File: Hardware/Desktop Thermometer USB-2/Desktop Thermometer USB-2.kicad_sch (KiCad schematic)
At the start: 0 parts

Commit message: Updated some symbols and footprints. Also added a new model for an epoxy type ceramic capacitor
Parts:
- added C1: C, Footprints:C_Epoxy_D5.5mm_W3.2mm_P5.00mm, symbol Schematic Symbols:C
- added J1: USB_TYPE_B, 00TH-Connector:USB_TYPE_B, symbol Schematic Symbols:USB_TYPE_B
- added R1: R, Resistor_THT:R_Axial_DIN0414_L11.9mm_D4.5mm_P15.24mm_Horizontal, symbol Device:R
- added U1: PIC16F15214, Footprints:DIP-8_W7.62mm_LongPads, symbol Schematic Symbols:PIC16F15214
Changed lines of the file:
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@@
 (kicad_sch (version 20230121) (generator eeschema)
   (paper "A4")
+  (symbol (lib_id "Schematic Symbols:USB_TYPE_B") (at 62.865 109.22 0) (unit 1)
+    (in_bom yes) (on_board yes) (dnp no) (fields_autoplaced)
+    (property "Reference" "J1" (at 62.865 96.52 0)
+      (effects (font (size 1.27 1.27)))
+    )
+    (property "Value" "USB_TYPE_B" (at 62.865 99.06 0)
+      (effects (font (size 1.27 1.27)))
+    )
+    (property "Footprint" "00TH-Connector:USB_TYPE_B" (at 62.865 133.35 0)
+      (effects (font (size 1.27 1.27)) hide)
+    )
+    (property "Datasheet" "https://www.cuidevices.com/product/resource/uj2-bh-th.pdf" (at 62.865 130.81 0)
+      (effects (font (size 1.27 1.27)) hide)
+    )
+    (pin "1")
+    (pin "2")
+    (pin "3")
+    (pin "5")
+    (pin "4")
+    (instances
+      (project "Desktop Thermometer USB-2"
+        (path "/155b486c-e28e-4d6b-9039-05edc3f4c6ee"
+          (reference "J1") (unit 1)
+        )
+      )
+    )
+  )
+  (symbol (lib_id "Schematic Symbols:PIC16F15214") (at 85.09 57.15 0) (unit 1)
+    (in_bom yes) (on_board yes) (dnp no)
+    (property "Reference" "U1" (at 78.74 46.99 0)
+      (effects (font (size 1.27 1.27)) (justify right))
+    )
+    (property "Value" "PIC16F15214" (at 91.44 67.31 0)
+      (effects (font (size 1.27 1.27)) (justify right))
+    )
+    (property "Footprint" "Footprints:DIP-8_W7.62mm_LongPads" (at 85.09 82.55 0)
+      (effects (font (size 1.27 1.27) italic) hide)
+    )
+    (property "Datasheet" "https://ww1.microchip.com/downloads/en/DeviceDoc/PIC16F15213-14-23-24-43-44-Data-Sheet-DS40002195B.pdf" (at 87.63 85.09 0)
+      (effects (font (size 1.27 1.27)) hide)
+    )
+    (pin "1")
+    (pin "6")
+    (pin "8")
+    (pin "7")
+    (pin "3")
+    (pin "2")
+    (pin "5")
+    (pin "4")
+    (instances
+      (project "Desktop Thermometer USB-2"
+        (path "/155b486c-e28e-4d6b-9039-05edc3f4c6ee"
+          (reference "U1") (unit 1)
+        )
+      )
+    )
+  )
+  (symbol (lib_id "power:GND") (at 196.85 93.98 0) (unit 1)
+    (in_bom yes) (on_board yes) (dnp no) (fields_autoplaced)
+    (property "Reference" "#PWR02" (at 196.85 100.33 0)
+      (effects (font (size 1.27 1.27)) hide)
+    )
+    (property "Value" "GND" (at 196.85 99.06 0)
+      (effects (font (size 1.27 1.27)))
+    )
+    (property "Footprint" "" (at 196.85 93.98 0)
+      (effects (font (size 1.27 1.27)) hide)
+    )
+    (property "Datasheet" "" (at 196.85 93.98 0)
+      (effects (font (size 1.27 1.27)) hide)
+    )
+    (pin "1")
+    (instances
+      (project "Desktop Thermometer USB-2"
+        (path "/155b486c-e28e-4d6b-9039-05edc3f4c6ee"
+          (reference "#PWR02") (unit 1)
+        )
+      )
+    )
+  )
+  (symbol (lib_id "Schematic Symbols:C") (at 121.92 92.71 0) (unit 1)
+    (in_bom yes) (on_board yes) (dnp no) (fields_autoplaced)
+    (property "Reference" "C1" (at 125.73 91.44 0)
+      (effects (font (size 1.27 1.27)) (justify left))
+    )
+    (property "Value" "C" (at 125.73 93.98 0)
+      (effects (font (size 1.27 1.27)) (justify left))
+    )
+    (property "Footprint" "Footprints:C_Epoxy_D5.5mm_W3.2mm_P5.00mm" (at 120.65 104.14 0)
+      (effects (font (size 1.27 1.27)) hide)
+    )
+    (property "Datasheet" "https://www.vishay.com/docs/45171/kseries.pdf" (at 120.65 106.68 0)
+      (effects (font (size 1.27 1.27)) hide)
+    )
+    (pin "1")
+    (pin "2")
+    (instances
+      (project "Desktop Thermometer USB-2"
+        (path "/155b486c-e28e-4d6b-9039-05edc3f4c6ee"
+          (reference "C1") (unit 1)
+        )
+      )
+    )
+  )
+  (symbol (lib_id "power:+5V") (at 207.645 71.12 0) (unit 1)
+    (in_bom yes) (on_board yes) (dnp no) (fields_autoplaced)
+    (property "Reference" "#PWR01" (at 207.645 74.93 0)
+      (effects (font (size 1.27 1.27)) hide)
+    )
+    (property "Value" "+5V" (at 207.645 66.04 0)
+      (effects (font (size 1.27 1.27)))
+    )
+    (property "Footprint" "" (at 207.645 71.12 0)
+      (effects (font (size 1.27 1.27)) hide)
+    )
+    (property "Datasheet" "" (at 207.645 71.12 0)
+      (effects (font (size 1.27 1.27)) hide)
+    )
+    (pin "1")
+    (instances
+      (project "Desktop Thermometer USB-2"
+        (path "/155b486c-e28e-4d6b-9039-05edc3f4c6ee"
+          (reference "#PWR01") (unit 1)
+        )
+      )
+    )
+  )
+  (symbol (lib_id "Device:R") (at 140.97 67.945 0) (unit 1)
+    (in_bom yes) (on_board yes) (dnp no) (fields_autoplaced)
+    (property "Reference" "R1" (at 143.51 66.675 0)
+      (effects (font (size 1.27 1.27)) (justify left))
+    )
+    (property "Value" "R" (at 143.51 69.215 0)
+      (effects (font (size 1.27 1.27)) (justify left))
+    )
+    (property "Footprint" "Resistor_THT:R_Axial_DIN0414_L11.9mm_D4.5mm_P15.24mm_Horizontal" (at 139.192 67.945 90)
+      (effects (font (size 1.27 1.27)) hide)
+    )
+    (property "Datasheet" "https://www.seielect.com/catalog/sei-cf_cfm.pdf" (at 140.97 67.945 0)
+      (effects (font (size 1.27 1.27)) hide)
+    )
+    (pin "1")
+    (pin "2")
+    (instances
+      (project "Desktop Thermometer USB-2"
+        (path "/155b486c-e28e-4d6b-9039-05edc3f4c6ee"
+          (reference "R1") (unit 1)
+        )
+      )
+    )
+  )
   (sheet_instances
     (path "/" (page "1"))

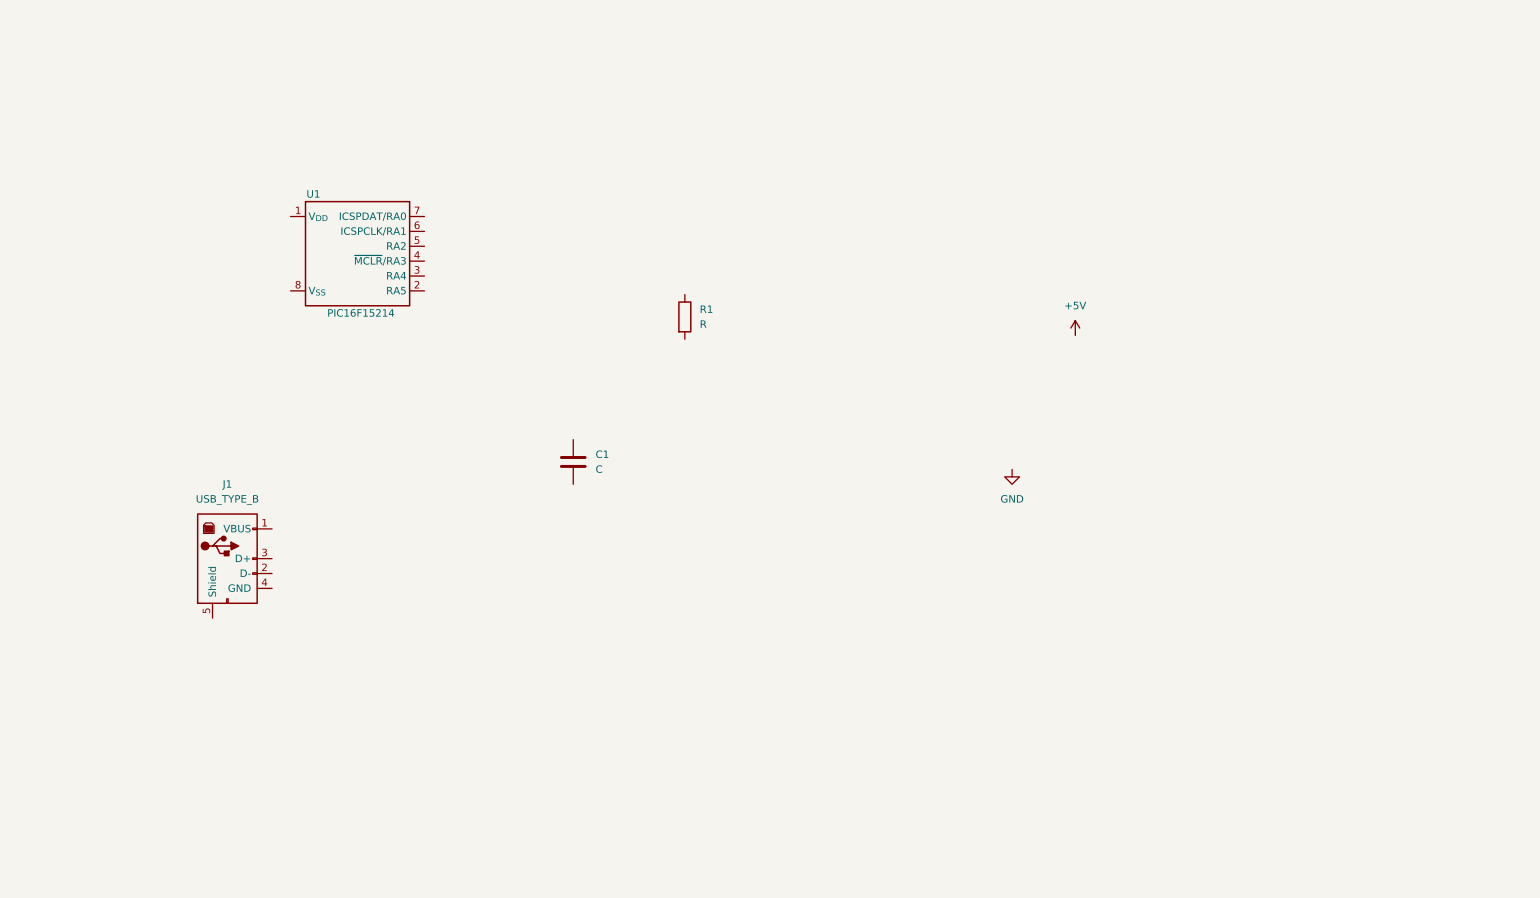
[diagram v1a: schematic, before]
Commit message: Schematic roughed out, requires a tidy up into sections. Added some more symbols and footprints...Hopefully done with that stuff!
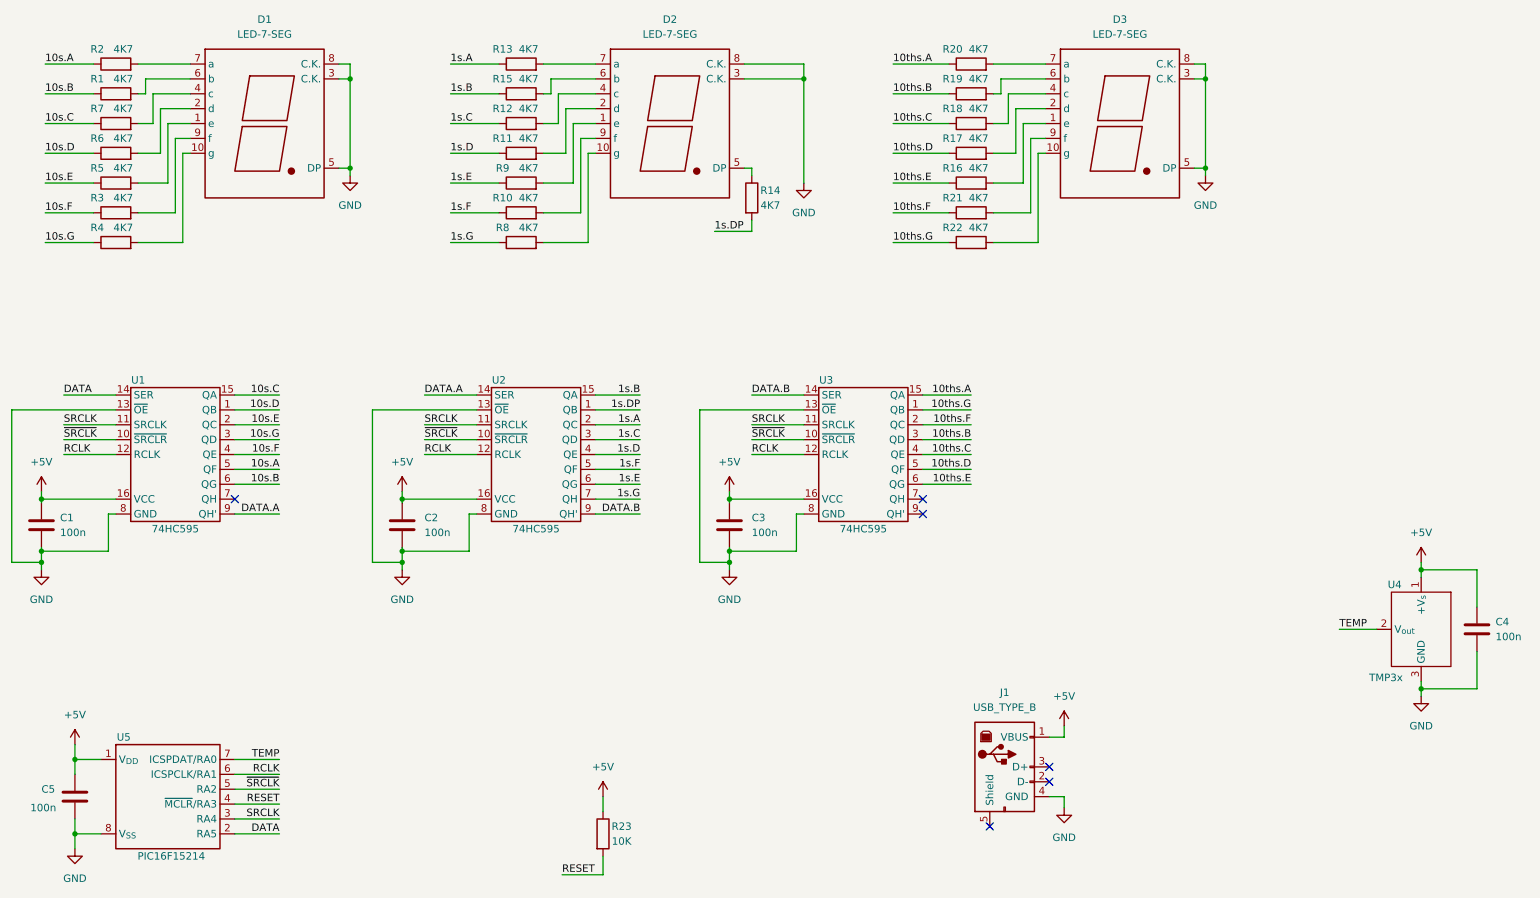
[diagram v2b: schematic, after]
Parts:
- removed U1: PIC16F15214, Footprints:DIP-8_W7.62mm_LongPads, symbol Schematic Symbols:PIC16F15214
- added C2, C3, C4, C5: 100n, Footprints:C_Epoxy_D5.5mm_W3.2mm_P5.00mm, symbol Schematic Symbols:C
- added D1, D2, D3: LED-7-SEG, Footprints:LED-7-SEG, symbol Schematic Symbols:LED-7-SEG
- added R10, R11, R12, R13, R14, R15, R16, R17, R18, R19, R2, R20, R21, R22, R3, R4, R5, R6, R7, R8, R9: 4K7, Resistor_THT:R_Axial_DIN0414_L11.9mm_D4.5mm_P15.24mm_Horizontal, symbol Device:R
- added R23: 10K, Resistor_THT:R_Axial_DIN0414_L11.9mm_D4.5mm_P15.24mm_Horizontal, symbol Device:R
- added U1, U2, U3: 74HC595, Footprints:DIP-16_W7.62mm_LongPads, symbol Schematic Symbols:74HC595
- added U4: TMP3x, Footprints:TMP3x_TO-92, symbol Schematic Symbols:TMP3x
- added U5: PIC16F15214, Footprints:DIP-8_W7.62mm_LongPads, symbol Schematic Symbols:PIC16F15214
- C1: value C -> 100n
- J1: footprint 00TH-Connector:USB_TYPE_B -> Footprints:USB_TYPE_B
- R1: value R -> 4K7
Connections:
- net +5V: now also C1.1, J1.1 (VBUS), C2.1, C3.1, C4.1, C5.1, R23.1, U1.16 (VCC), U2.16 (VCC), U3.16 (VCC), U4.1 (+V_{s}), U5.1 (V_{DD})
- net GND: now also C1.2, J1.4 (GND), C2.2, C3.2, C4.2, C5.2, D1.3 (C.K.), D1.5 (DP), D1.8 (C.K.), D2.3 (C.K.), D2.8 (C.K.), D3.3 (C.K.), D3.5 (DP), D3.8 (C.K.), U1.13 (~{OE}), U1.8 (GND), U2.13 (~{OE}), U2.8 (GND), U3.13 (~{OE}), U3.8 (GND), U4.3 (GND), U5.8 (V_{SS})
- net 10s.B: now reaches R1.1
- net 10s.B: now also U1.6 (QG)
- net at R1.2: now also D1.6 (b)
- new net: D2.6 (b), R15.2
- new net: D2.4 (c), R12.2
- new net: D2.5 (DP), R14.1
- new net: D2.1 (e), R9.2
- new net: D2.10 (g), R8.2
- new net: D2.2 (d), R11.2
- new net: D2.7 (a), R13.2
- new net: D2.9 (f), R10.2
- new net: D1.2 (d), R6.2
- new net: D3.1 (e), R16.2
- new net: D1.1 (e), R5.2
- new net: D1.10 (g), R4.2
- new net: D1.4 (c), R7.2
- new net: D1.7 (a), R2.2
- new net: D1.9 (f), R3.2
- new net: D3.2 (d), R17.2
- new net: D3.6 (b), R19.2
- new net: D3.10 (g), R22.2
- new net: D3.9 (f), R21.2
- new net: D3.4 (c), R18.2
- new net: D3.7 (a), R20.2
- new net 10s.A: R2.1, U1.5 (QF)
- new net 10s.C: R7.1, U1.15 (QA)
- new net 10s.D: R6.1, U1.1 (QB)
- new net 10s.E: R5.1, U1.2 (QC)
- new net 10s.F: R3.1, U1.4 (QE)
- new net 10s.G: R4.1, U1.3 (QD)
- new net 10ths.A: R20.1, U3.15 (QA)
- new net 10ths.B: R19.1, U3.3 (QD)
- new net 10ths.C: R18.1, U3.4 (QE)
- new net 10ths.D: R17.1, U3.5 (QF)
- new net 10ths.E: R16.1, U3.6 (QG)
- new net 10ths.F: R21.1, U3.2 (QC)
- new net 10ths.G: R22.1, U3.1 (QB)
- new net 1s.A: R13.1, U2.2 (QC)
- new net 1s.B: R15.1, U2.15 (QA)
- new net 1s.C: R12.1, U2.3 (QD)
- new net 1s.D: R11.1, U2.4 (QE)
- new net 1s.DP: R14.2, U2.1 (QB)
- new net 1s.E: R9.1, U2.6 (QG)
- new net 1s.F: R10.1, U2.5 (QF)
- new net 1s.G: R8.1, U2.7 (QH)
- new net DATA: U1.14 (SER), U5.2 (RA5)
- new net DATA.A: U1.9 (QH'), U2.14 (SER)
- new net DATA.B: U2.9 (QH'), U3.14 (SER)
- new net RCLK: U1.12 (RCLK), U2.12 (RCLK), U3.12 (RCLK), U5.6 (ICSPCLK/RA1)
- new net RESET: R23.2, U5.4 (~{MCLR}/RA3)
- new net SRCLK: U1.11 (SRCLK), U2.11 (SRCLK), U3.11 (SRCLK), U5.3 (RA4)
- new net TEMP: U4.2 (V_{out}), U5.7 (ICSPDAT/RA0)
- new net ~{SRCLK}: U1.10 (~{SRCLR}), U2.10 (~{SRCLR}), U3.10 (~{SRCLR}), U5.5 (RA2)
- no-connect marks 0 -> 6
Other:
- title: (none) -> Desktop Thermometer - USB 2 Version

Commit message: Initial attempt of PCB layout
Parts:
- R1, R10, R11, R12, R13, R14, R15, R16, R17, R18, R19, R2, R20, R21, R22, R23, R3, R4, R5, R6, R7, R8, R9: footprint Resistor_THT:R_Axial_DIN0414_L11.9mm_D4.5mm_P15.24mm_Horizontal -> Resistor_THT:R_Axial_DIN0207_L6.3mm_D2.5mm_P10.16mm_Horizontal
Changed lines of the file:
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@@
       (effects (font (size 1.27 1.27)))
     )
-    (property "Footprint" "Resistor_THT:R_Axial_DIN0414_L11.9mm_D4.5mm_P15.24mm_Horizontal" (at 113.03 31.623 90)
+    (property "Footprint" "Resistor_THT:R_Axial_DIN0207_L6.3mm_D2.5mm_P10.16mm_Horizontal" (at 113.03 31.623 90)
       (effects (font (size 1.27 1.27)) hide)
     )
@@
       (effects (font (size 1.27 1.27)))
     )
-    (property "Footprint" "Resistor_THT:R_Axial_DIN0414_L11.9mm_D4.5mm_P15.24mm_Horizontal" (at 113.03 36.703 90)
+    (property "Footprint" "Resistor_THT:R_Axial_DIN0207_L6.3mm_D2.5mm_P10.16mm_Horizontal" (at 113.03 36.703 90)
       (effects (font (size 1.27 1.27)) hide)
     )
@@
       (effects (font (size 1.27 1.27)))
     )
-    (property "Footprint" "Resistor_THT:R_Axial_DIN0414_L11.9mm_D4.5mm_P15.24mm_Horizontal" (at 150.622 47.625 90)
+    (property "Footprint" "Resistor_THT:R_Axial_DIN0207_L6.3mm_D2.5mm_P10.16mm_Horizontal" (at 150.622 47.625 90)
       (effects (font (size 1.27 1.27)) hide)
     )
@@
       (effects (font (size 1.27 1.27)))
     )
-    (property "Footprint" "Resistor_THT:R_Axial_DIN0414_L11.9mm_D4.5mm_P15.24mm_Horizontal" (at 113.03 26.543 90)
+    (property "Footprint" "Resistor_THT:R_Axial_DIN0207_L6.3mm_D2.5mm_P10.16mm_Horizontal" (at 113.03 26.543 90)
       (effects (font (size 1.27 1.27)) hide)
     )
@@
       (effects (font (size 1.27 1.27)))
     )
-    (property "Footprint" "Resistor_THT:R_Axial_DIN0414_L11.9mm_D4.5mm_P15.24mm_Horizontal" (at 43.815 41.783 90)
+    (property "Footprint" "Resistor_THT:R_Axial_DIN0207_L6.3mm_D2.5mm_P10.16mm_Horizontal" (at 43.815 41.783 90)
       (effects (font (size 1.27 1.27)) hide)
     )
@@
       (effects (font (size 1.27 1.27)))
     )
-    (property "Footprint" "Resistor_THT:R_Axial_DIN0414_L11.9mm_D4.5mm_P15.24mm_Horizontal" (at 189.865 46.863 90)
+    (property "Footprint" "Resistor_THT:R_Axial_DIN0207_L6.3mm_D2.5mm_P10.16mm_Horizontal" (at 189.865 46.863 90)
       (effects (font (size 1.27 1.27)) hide)
     )
@@
       (effects (font (size 1.27 1.27)))
     )
-    (property "Footprint" "Resistor_THT:R_Axial_DIN0414_L11.9mm_D4.5mm_P15.24mm_Horizontal" (at 189.865 41.783 90)
+    (property "Footprint" "Resistor_THT:R_Axial_DIN0207_L6.3mm_D2.5mm_P10.16mm_Horizontal" (at 189.865 41.783 90)
       (effects (font (size 1.27 1.27)) hide)
     )
@@
       (effects (font (size 1.27 1.27)))
     )
-    (property "Footprint" "Resistor_THT:R_Axial_DIN0414_L11.9mm_D4.5mm_P15.24mm_Horizontal" (at 43.815 26.543 90)
+    (property "Footprint" "Resistor_THT:R_Axial_DIN0207_L6.3mm_D2.5mm_P10.16mm_Horizontal" (at 43.815 26.543 90)
       (effects (font (size 1.27 1.27)) hide)
     )
@@
       (effects (font (size 1.27 1.27)))
     )
-    (property "Footprint" "Resistor_THT:R_Axial_DIN0414_L11.9mm_D4.5mm_P15.24mm_Horizontal" (at 125.222 156.21 90)
+    (property "Footprint" "Resistor_THT:R_Axial_DIN0207_L6.3mm_D2.5mm_P10.16mm_Horizontal" (at 125.222 156.21 90)
       (effects (font (size 1.27 1.27)) hide)
     )
@@
       (effects (font (size 1.27 1.27)))
     )
-    (property "Footprint" "Resistor_THT:R_Axial_DIN0414_L11.9mm_D4.5mm_P15.24mm_Horizontal" (at 43.815 31.623 90)
+    (property "Footprint" "Resistor_THT:R_Axial_DIN0207_L6.3mm_D2.5mm_P10.16mm_Horizontal" (at 43.815 31.623 90)
       (effects (font (size 1.27 1.27)) hide)
     )
@@
       (effects (font (size 1.27 1.27)))
     )
-    (property "Footprint" "Resistor_THT:R_Axial_DIN0414_L11.9mm_D4.5mm_P15.24mm_Horizontal" (at 43.815 46.863 90)
+    (property "Footprint" "Resistor_THT:R_Axial_DIN0207_L6.3mm_D2.5mm_P10.16mm_Horizontal" (at 43.815 46.863 90)
       (effects (font (size 1.27 1.27)) hide)
     )
@@
       (effects (font (size 1.27 1.27)))
     )
-    (property "Footprint" "Resistor_THT:R_Axial_DIN0414_L11.9mm_D4.5mm_P15.24mm_Horizontal" (at 43.815 57.023 90)
+    (property "Footprint" "Resistor_THT:R_Axial_DIN0207_L6.3mm_D2.5mm_P10.16mm_Horizontal" (at 43.815 57.023 90)
       (effects (font (size 1.27 1.27)) hide)
     )
@@
       (effects (font (size 1.27 1.27)))
     )
-    (property "Footprint" "Resistor_THT:R_Axial_DIN0414_L11.9mm_D4.5mm_P15.24mm_Horizontal" (at 189.865 31.623 90)
+    (property "Footprint" "Resistor_THT:R_Axial_DIN0207_L6.3mm_D2.5mm_P10.16mm_Horizontal" (at 189.865 31.623 90)
       (effects (font (size 1.27 1.27)) hide)
     )
@@
       (effects (font (size 1.27 1.27)))
     )
-    (property "Footprint" "Resistor_THT:R_Axial_DIN0414_L11.9mm_D4.5mm_P15.24mm_Horizontal" (at 189.865 57.023 90)
+    (property "Footprint" "Resistor_THT:R_Axial_DIN0207_L6.3mm_D2.5mm_P10.16mm_Horizontal" (at 189.865 57.023 90)
       (effects (font (size 1.27 1.27)) hide)
     )
@@
       (effects (font (size 1.27 1.27)))
     )
-    (property "Footprint" "Resistor_THT:R_Axial_DIN0414_L11.9mm_D4.5mm_P15.24mm_Horizontal" (at 189.865 51.943 90)
+    (property "Footprint" "Resistor_THT:R_Axial_DIN0207_L6.3mm_D2.5mm_P10.16mm_Horizontal" (at 189.865 51.943 90)
       (effects (font (size 1.27 1.27)) hide)
     )
@@
       (effects (font (size 1.27 1.27)))
     )
-    (property "Footprint" "Resistor_THT:R_Axial_DIN0414_L11.9mm_D4.5mm_P15.24mm_Horizontal" (at 113.03 46.863 90)
+    (property "Footprint" "Resistor_THT:R_Axial_DIN0207_L6.3mm_D2.5mm_P10.16mm_Horizontal" (at 113.03 46.863 90)
       (effects (font (size 1.27 1.27)) hide)
     )
@@
       (effects (font (size 1.27 1.27)))
     )
-    (property "Footprint" "Resistor_THT:R_Axial_DIN0414_L11.9mm_D4.5mm_P15.24mm_Horizontal" (at 113.03 51.943 90)
+    (property "Footprint" "Resistor_THT:R_Axial_DIN0207_L6.3mm_D2.5mm_P10.16mm_Horizontal" (at 113.03 51.943 90)
       (effects (font (size 1.27 1.27)) hide)
     )
@@
       (effects (font (size 1.27 1.27)))
     )
-    (property "Footprint" "Resistor_THT:R_Axial_DIN0414_L11.9mm_D4.5mm_P15.24mm_Horizontal" (at 43.815 51.943 90)
+    (property "Footprint" "Resistor_THT:R_Axial_DIN0207_L6.3mm_D2.5mm_P10.16mm_Horizontal" (at 43.815 51.943 90)
       (effects (font (size 1.27 1.27)) hide)
     )
@@
       (effects (font (size 1.27 1.27)))
     )
-    (property "Footprint" "Resistor_THT:R_Axial_DIN0414_L11.9mm_D4.5mm_P15.24mm_Horizontal" (at 43.815 36.703 90)
+    (property "Footprint" "Resistor_THT:R_Axial_DIN0207_L6.3mm_D2.5mm_P10.16mm_Horizontal" (at 43.815 36.703 90)
       (effects (font (size 1.27 1.27)) hide)
     )
@@
       (effects (font (size 1.27 1.27)))
     )
-    (property "Footprint" "Resistor_THT:R_Axial_DIN0414_L11.9mm_D4.5mm_P15.24mm_Horizontal" (at 113.03 41.783 90)
+    (property "Footprint" "Resistor_THT:R_Axial_DIN0207_L6.3mm_D2.5mm_P10.16mm_Horizontal" (at 113.03 41.783 90)
       (effects (font (size 1.27 1.27)) hide)
     )
@@
       (effects (font (size 1.27 1.27)))
     )
-    (property "Footprint" "Resistor_THT:R_Axial_DIN0414_L11.9mm_D4.5mm_P15.24mm_Horizontal" (at 113.03 57.023 90)
+    (property "Footprint" "Resistor_THT:R_Axial_DIN0207_L6.3mm_D2.5mm_P10.16mm_Horizontal" (at 113.03 57.023 90)
       (effects (font (size 1.27 1.27)) hide)
     )
@@
       (effects (font (size 1.27 1.27)))
     )
-    (property "Footprint" "Resistor_THT:R_Axial_DIN0414_L11.9mm_D4.5mm_P15.24mm_Horizontal" (at 189.865 36.703 90)
+    (property "Footprint" "Resistor_THT:R_Axial_DIN0207_L6.3mm_D2.5mm_P10.16mm_Horizontal" (at 189.865 36.703 90)
       (effects (font (size 1.27 1.27)) hide)
     )
@@
       (effects (font (size 1.27 1.27)))
     )
-    (property "Footprint" "Resistor_THT:R_Axial_DIN0414_L11.9mm_D4.5mm_P15.24mm_Horizontal" (at 189.865 26.543 90)
-      (effects (font (size 1.27 1.27)) hide)
-    )
+    (property "Footprint" "Resistor_THT:R_Axial_DIN0207_L6.3mm_D2.5mm_P10.16mm_Horizontal" (at 189.865 26.543 90)
+      (effects (font (size 1.27 1.27)) hide)
+    )
